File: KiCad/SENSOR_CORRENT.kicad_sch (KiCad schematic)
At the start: 4 parts, among them J1 Conn_01x08_Pin, SW1 SS-1GL2-F-D

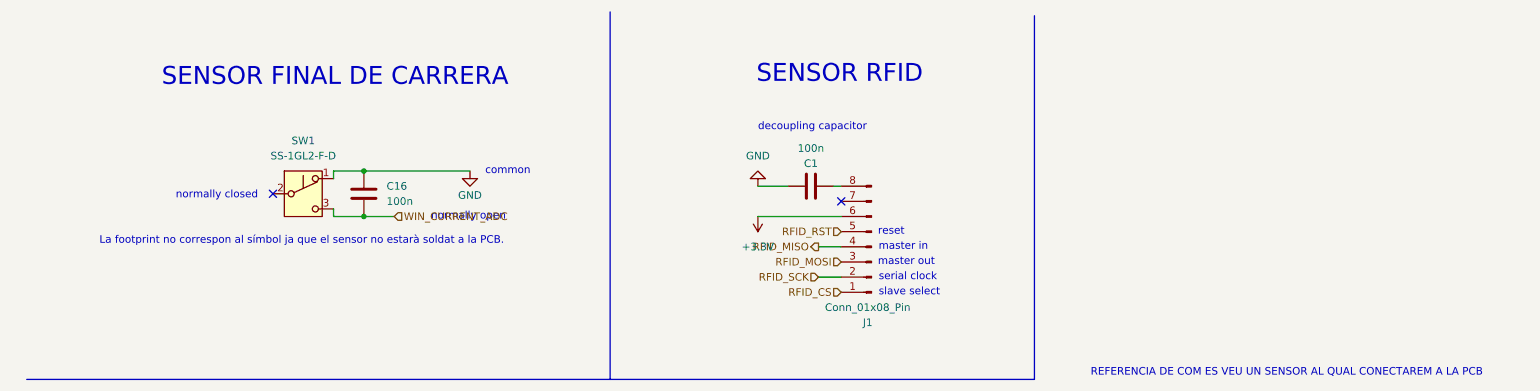
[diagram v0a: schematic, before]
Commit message: Actulitació de components
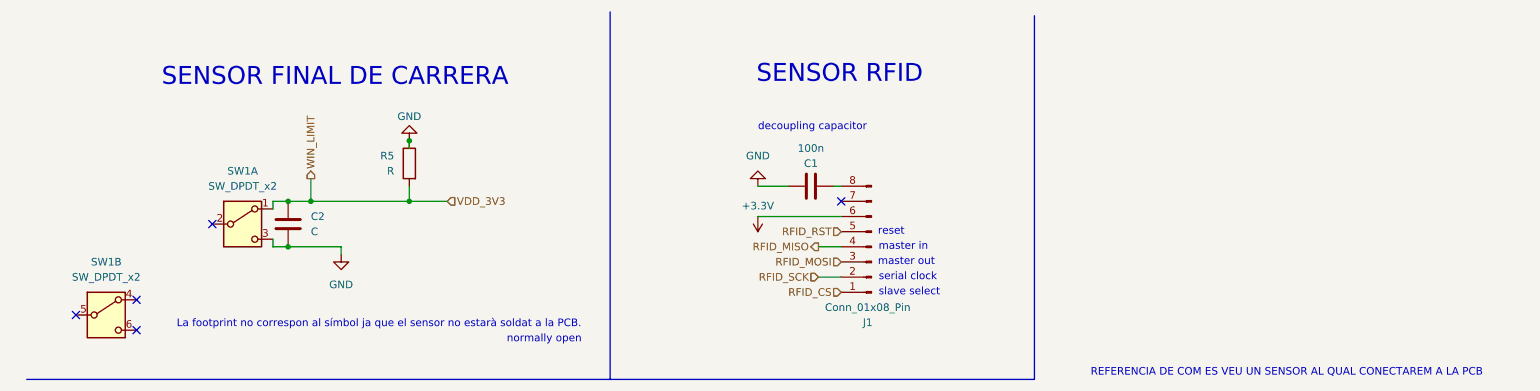
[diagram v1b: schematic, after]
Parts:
- removed C16: 100n, Capacitor_SMD:C_0805_2012Metric, symbol Device:C
- removed SW1: SS-1GL2-F-D, Connector_PinSocket_1.00mm:PinSocket_1x03_P1.00mm_Vertical, symbol Switch:SW_Push_SPDT
- added C2: C, symbol Device:C
- added R5: R, symbol Device:R
- added SW1: SW_DPDT_x2, Button_Switch_SMD:SW_DPDT_CK_JS202011JCQN, symbol Switch:SW_DPDT_x2
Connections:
- net GND: now also C2.2, R5.1, SW1.3 (C)
- new net VDD_3V3: C2.1, R5.2, SW1.1 (A)
- no-connect marks 2 -> 5
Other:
- note removed: "common"
- note removed: "normally closed"

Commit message: Recover
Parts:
- C2: value C -> 100nF
- R5: value R -> 10k
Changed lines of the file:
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@@
 		(color 0 0 0 0)
 	)
-	(junction
-		(at 76.2 33.02)
-		(diameter 0)
-		(color 0 0 0 0)
-	)
 	(no_connect
 		(at 20.32 62.23)
@@
 		(fields_autoplaced yes)
 		(property "Reference" "R5"
-			(at 73.66 35.5599 0)
+			(at 78.74 35.5599 0)
 			(effects
 				(font
 					(size 1.27 1.27)
 				)
-				(justify left)
+				(justify right)
 			)
 		)
-		(property "Value" "R"
-			(at 73.66 38.0999 0)
+		(property "Value" "10k"
+			(at 78.74 38.0999 0)
 			(effects
 				(font
 					(size 1.27 1.27)
 				)
-				(justify left)
+				(justify right)
 			)
 		)
@@
 			)
 		)
-		(property "Value" "C"
+		(property "Value" "100nF"
 			(at 59.69 48.2599 0)
 			(effects
